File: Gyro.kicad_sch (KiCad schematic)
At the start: 5 parts, among them U4 MPU-6050

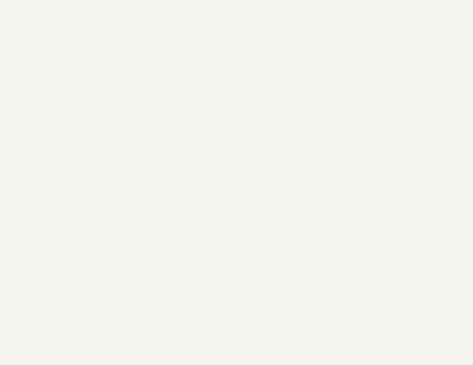
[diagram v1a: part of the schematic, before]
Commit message: MCU interfaces are done! Check the Changes and Complete ERC modifications
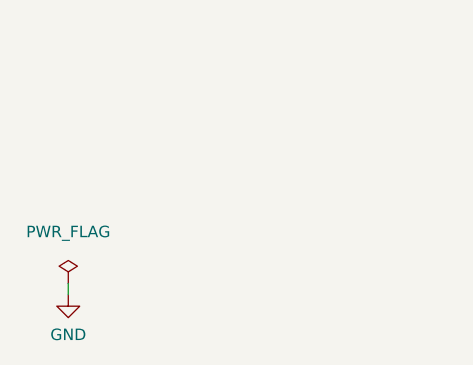
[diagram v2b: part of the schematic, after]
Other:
- company: (none) -> Parikshit Student Satellite Team
- title: (none) -> AOCS BOARD
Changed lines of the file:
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@@
 (kicad_sch (version 20211123) (generator eeschema)
   (paper "A4")
+  (title_block
+    (title "AOCS BOARD")
+    (company "Parikshit Student Satellite Team")
+  )
   (junction (at 113.03 90.17) (diameter 0) (color 0 0 0 0)
   )
@@
   (no_connect (at 151.13 74.93))
   (no_connect (at 151.13 80.01))
+  (wire (pts (xy 27.94 147.32) (xy 27.94 146.05))
+    (stroke (width 0) (type default) (color 0 0 0 0))
+  )
   (wire (pts (xy 114.3 43.18) (xy 114.3 46.99))
     (stroke (width 0) (type default) (color 0 0 0 0))
@@
       (effects (font (size 1.27 1.27)) hide)
     )
+    (pin "1")
+  )
+  (symbol (lib_id "power:PWR_FLAG") (at 27.94 146.05 0) (unit 1)
+    (in_bom yes) (on_board yes) (fields_autoplaced)
+    (property "Reference" "#FLG0107" (id 0) (at 27.94 144.145 0)
+      (effects (font (size 1.27 1.27)) hide)
+    )
+    (property "Value" "PWR_FLAG" (id 1) (at 27.94 140.335 0))
+    (property "Footprint" "" (id 2) (at 27.94 146.05 0)
+      (effects (font (size 1.27 1.27)) hide)
+    )
+    (property "Datasheet" "~" (id 3) (at 27.94 146.05 0)
+      (effects (font (size 1.27 1.27)) hide)
+    )
+    (pin "1")
+  )
+  (symbol (lib_id "power:GND") (at 27.94 147.32 0) (unit 1)
+    (in_bom yes) (on_board yes) (fields_autoplaced)
+    (property "Reference" "#PWR0271" (id 0) (at 27.94 153.67 0)
+      (effects (font (size 1.27 1.27)) hide)
+    )
+    (property "Value" "GND" (id 1) (at 27.94 151.765 0))
+    (property "Footprint" "" (id 2) (at 27.94 147.32 0)
+      (effects (font (size 1.27 1.27)) hide)
+    )
+    (property "Datasheet" "" (id 3) (at 27.94 147.32 0)
+      (effects (font (size 1.27 1.27)) hide)
+    )

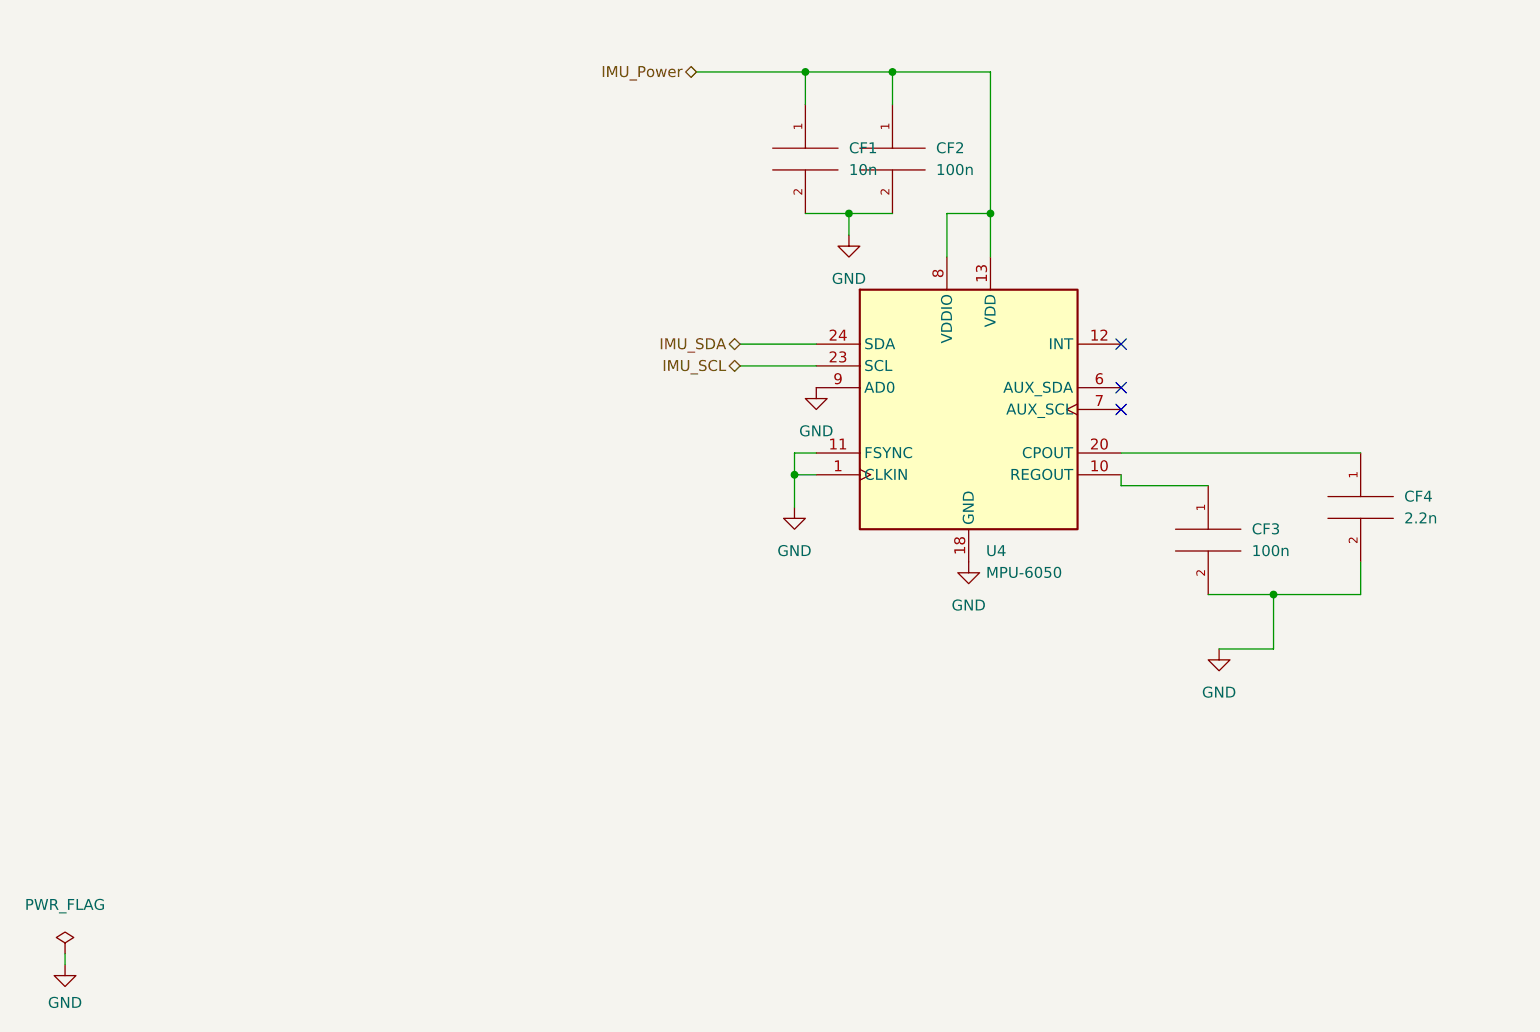
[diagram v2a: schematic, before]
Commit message: Max ERC errors corrected
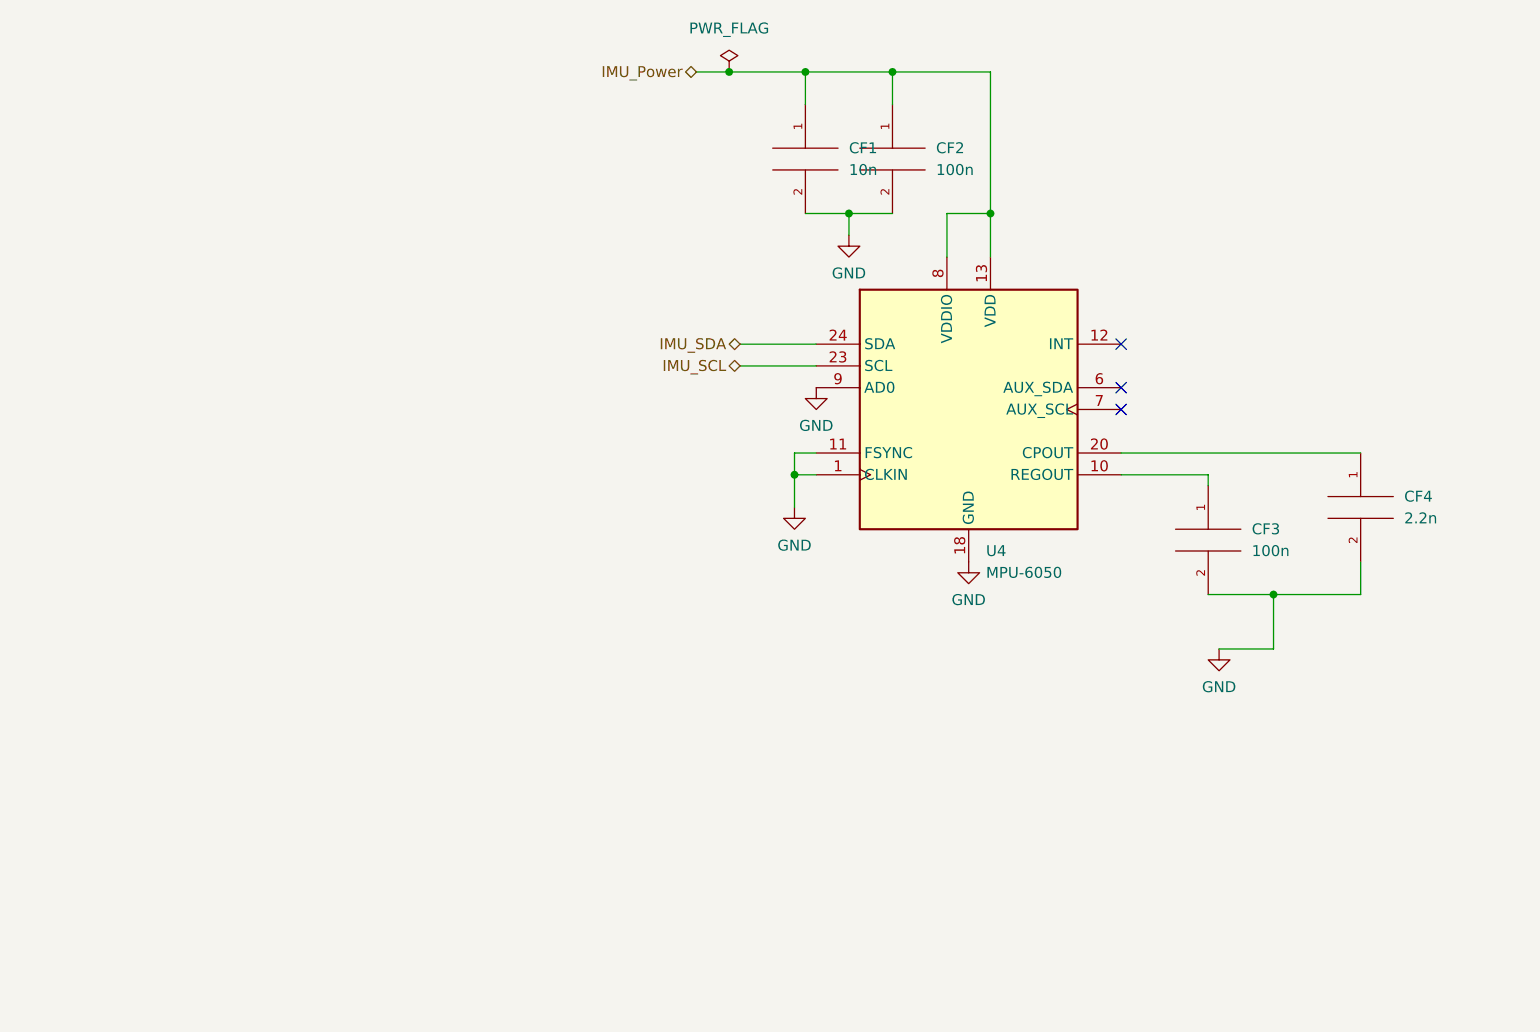
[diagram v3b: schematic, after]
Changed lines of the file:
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@@
   (junction (at 135.89 59.69) (diameter 0) (color 0 0 0 0)
+  )
+  (junction (at 105.41 43.18) (diameter 0) (color 0 0 0 0)
   )
   (junction (at 119.38 59.69) (diameter 0) (color 0 0 0 0)
@@
   (no_connect (at 151.13 74.93))
   (no_connect (at 151.13 80.01))
-  (wire (pts (xy 27.94 147.32) (xy 27.94 146.05))
-    (stroke (width 0) (type default) (color 0 0 0 0))
-  )
   (wire (pts (xy 114.3 43.18) (xy 114.3 46.99))
     (stroke (width 0) (type default) (color 0 0 0 0))
@@
     (stroke (width 0) (type default) (color 0 0 0 0))
   )
-  (wire (pts (xy 151.13 91.44) (xy 151.13 90.17))
-    (stroke (width 0) (type default) (color 0 0 0 0))
-  )
   (wire (pts (xy 114.3 59.69) (xy 119.38 59.69))
     (stroke (width 0) (type default) (color 0 0 0 0))
@@
     (stroke (width 0) (type default) (color 0 0 0 0))
   )
-  (wire (pts (xy 101.6 43.18) (xy 114.3 43.18))
+  (wire (pts (xy 101.6 43.18) (xy 105.41 43.18))
     (stroke (width 0) (type default) (color 0 0 0 0))
   )
@@
     (stroke (width 0) (type default) (color 0 0 0 0))
   )
+  (wire (pts (xy 105.41 43.18) (xy 114.3 43.18))
+    (stroke (width 0) (type default) (color 0 0 0 0))
+  )
   (wire (pts (xy 151.13 87.63) (xy 179.07 87.63))
     (stroke (width 0) (type default) (color 0 0 0 0))
@@
     (stroke (width 0) (type default) (color 0 0 0 0))
   )
-  (wire (pts (xy 161.29 91.44) (xy 151.13 91.44))
+  (wire (pts (xy 161.29 90.17) (xy 161.29 91.44))
+    (stroke (width 0) (type default) (color 0 0 0 0))
+  )
+  (wire (pts (xy 161.29 90.17) (xy 151.13 90.17))
     (stroke (width 0) (type default) (color 0 0 0 0))
   )
@@
     (pin "2")
   )
+  (symbol (lib_id "upsat-comms-hardware:GND") (at 162.56 110.49 0) (unit 1)
+    (in_bom yes) (on_board yes) (fields_autoplaced)
+    (property "Reference" "#PWR0163" (id 0) (at 162.56 116.84 0)
+      (effects (font (size 1.27 1.27)) hide)
+    )
+    (property "Value" "GND" (id 1) (at 162.56 114.935 0))
+    (property "Footprint" "" (id 2) (at 162.56 110.49 0))
+    (property "Datasheet" "" (id 3) (at 162.56 110.49 0))
+    (pin "1")
+  )
   (symbol (lib_id "pspice:C") (at 124.46 53.34 0) (unit 1)
     (in_bom yes) (on_board yes) (fields_autoplaced)
@@
     (pin "2")
   )
-  (symbol (lib_id "power:GND") (at 115.57 80.01 0) (unit 1)
-    (in_bom yes) (on_board yes) (fields_autoplaced)
-    (property "Reference" "#PWR0163" (id 0) (at 115.57 86.36 0)
-      (effects (font (size 1.27 1.27)) hide)
-    )
-    (property "Value" "GND" (id 1) (at 115.57 85.09 0))
-    (property "Footprint" "" (id 2) (at 115.57 80.01 0)
-      (effects (font (size 1.27 1.27)) hide)
-    )
-    (property "Datasheet" "" (id 3) (at 115.57 80.01 0)
-      (effects (font (size 1.27 1.27)) hide)
-    )
+  (symbol (lib_id "power:PWR_FLAG") (at 105.41 43.18 0) (unit 1)
+    (in_bom yes) (on_board yes) (fields_autoplaced)
+    (property "Reference" "#FLG0105" (id 0) (at 105.41 41.275 0)
+      (effects (font (size 1.27 1.27)) hide)
+    )
+    (property "Value" "PWR_FLAG" (id 1) (at 105.41 38.1 0))
+    (property "Footprint" "" (id 2) (at 105.41 43.18 0)
+      (effects (font (size 1.27 1.27)) hide)
+    )
+    (property "Datasheet" "~" (id 3) (at 105.41 43.18 0)
+      (effects (font (size 1.27 1.27)) hide)
+    )
+    (pin "1")
+  )
+  (symbol (lib_id "upsat-comms-hardware:GND") (at 113.03 93.98 0) (unit 1)
+    (in_bom yes) (on_board yes) (fields_autoplaced)
+    (property "Reference" "#PWR0166" (id 0) (at 113.03 100.33 0)
+      (effects (font (size 1.27 1.27)) hide)
+    )
+    (property "Value" "GND" (id 1) (at 113.03 98.425 0))
+    (property "Footprint" "" (id 2) (at 113.03 93.98 0))
+    (property "Datasheet" "" (id 3) (at 113.03 93.98 0))
+    (pin "1")
+  )
+  (symbol (lib_id "upsat-comms-hardware:GND") (at 115.57 80.01 0) (unit 1)
+    (in_bom yes) (on_board yes) (fields_autoplaced)
+    (property "Reference" "#PWR0165" (id 0) (at 115.57 86.36 0)
+      (effects (font (size 1.27 1.27)) hide)
+    )
+    (property "Value" "GND" (id 1) (at 115.57 84.455 0))
+    (property "Footprint" "" (id 2) (at 115.57 80.01 0))
+    (property "Datasheet" "" (id 3) (at 115.57 80.01 0))
     (pin "1")
   )
@@
     (pin "2")
   )
-  (symbol (lib_id "power:GND") (at 162.56 110.49 0) (unit 1)
-    (in_bom yes) (on_board yes) (fields_autoplaced)
-    (property "Reference" "#PWR0164" (id 0) (at 162.56 116.84 0)
-      (effects (font (size 1.27 1.27)) hide)
-    )
-    (property "Value" "GND" (id 1) (at 162.56 115.57 0))
-    (property "Footprint" "" (id 2) (at 162.56 110.49 0)
-      (effects (font (size 1.27 1.27)) hide)
-    )
-    (property "Datasheet" "" (id 3) (at 162.56 110.49 0)
-      (effects (font (size 1.27 1.27)) hide)
-    )
-    (pin "1")
-  )
-  (symbol (lib_id "power:GND") (at 133.35 100.33 0) (unit 1)
-    (in_bom yes) (on_board yes) (fields_autoplaced)
-    (property "Reference" "#PWR0166" (id 0) (at 133.35 106.68 0)
-      (effects (font (size 1.27 1.27)) hide)
-    )
-    (property "Value" "GND" (id 1) (at 133.35 105.41 0))
-    (property "Footprint" "" (id 2) (at 133.35 100.33 0)
-      (effects (font (size 1.27 1.27)) hide)
-    )
-    (property "Datasheet" "" (id 3) (at 133.35 100.33 0)
-      (effects (font (size 1.27 1.27)) hide)
-    )
-    (pin "1")
-  )
-  (symbol (lib_id "power:GND") (at 119.38 62.23 0) (unit 1)
+  (symbol (lib_id "upsat-comms-hardware:GND") (at 119.38 62.23 0) (unit 1)
     (in_bom yes) (on_board yes) (fields_autoplaced)
     (property "Reference" "#PWR0162" (id 0) (at 119.38 68.58 0)
       (effects (font (size 1.27 1.27)) hide)
     )
-    (property "Value" "GND" (id 1) (at 119.38 67.31 0))
-    (property "Footprint" "" (id 2) (at 119.38 62.23 0)
-      (effects (font (size 1.27 1.27)) hide)
-    )
-    (property "Datasheet" "" (id 3) (at 119.38 62.23 0)
-      (effects (font (size 1.27 1.27)) hide)
-    )
-    (pin "1")
-  )
-  (symbol (lib_id "power:GND") (at 113.03 93.98 0) (unit 1)
-    (in_bom yes) (on_board yes) (fields_autoplaced)
-    (property "Reference" "#PWR0165" (id 0) (at 113.03 100.33 0)
-      (effects (font (size 1.27 1.27)) hide)
-    )
-    (property "Value" "GND" (id 1) (at 113.03 99.06 0))
-    (property "Footprint" "" (id 2) (at 113.03 93.98 0)
-      (effects (font (size 1.27 1.27)) hide)
-    )
-    (property "Datasheet" "" (id 3) (at 113.03 93.98 0)
-      (effects (font (size 1.27 1.27)) hide)
-    )
-    (pin "1")
-  )
-  (symbol (lib_id "power:PWR_FLAG") (at 27.94 146.05 0) (unit 1)
-    (in_bom yes) (on_board yes) (fields_autoplaced)
-    (property "Reference" "#FLG0107" (id 0) (at 27.94 144.145 0)
-      (effects (font (size 1.27 1.27)) hide)
-    )
-    (property "Value" "PWR_FLAG" (id 1) (at 27.94 140.335 0))
-    (property "Footprint" "" (id 2) (at 27.94 146.05 0)
-      (effects (font (size 1.27 1.27)) hide)
-    )
-    (property "Datasheet" "~" (id 3) (at 27.94 146.05 0)
-      (effects (font (size 1.27 1.27)) hide)
-    )
-    (pin "1")
-  )
-  (symbol (lib_id "power:GND") (at 27.94 147.32 0) (unit 1)
-    (in_bom yes) (on_board yes) (fields_autoplaced)
-    (property "Reference" "#PWR0271" (id 0) (at 27.94 153.67 0)
-      (effects (font (size 1.27 1.27)) hide)
-    )
-    (property "Value" "GND" (id 1) (at 27.94 151.765 0))
-    (property "Footprint" "" (id 2) (at 27.94 147.32 0)
-      (effects (font (size 1.27 1.27)) hide)
-    )
-    (property "Datasheet" "" (id 3) (at 27.94 147.32 0)
-      (effects (font (size 1.27 1.27)) hide)
-    )
-    (pin "1")
-  )
+    (property "Value" "GND" (id 1) (at 119.38 66.675 0))
+    (property "Footprint" "" (id 2) (at 119.38 62.23 0))
+    (property "Datasheet" "" (id 3) (at 119.38 62.23 0))
+    (pin "1")
+  )
+  (symbol (lib_id "upsat-comms-hardware:GND") (at 133.35 100.33 0) (unit 1)
+    (in_bom yes) (on_board yes) (fields_autoplaced)
+    (property "Reference" "#PWR0164" (id 0) (at 133.35 106.68 0)
+      (effects (font (size 1.27 1.27)) hide)
+    )
+    (property "Value" "GND" (id 1) (at 133.35 104.775 0))
+    (property "Footprint" "" (id 2) (at 133.35 100.33 0))
+    (property "Datasheet" "" (id 3) (at 133.35 100.33 0))
+    (pin "1")
+  )

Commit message: Updated the changes
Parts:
- renumbered CF4 to CF3, CF3 to CF4
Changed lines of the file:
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@@
   (symbol (lib_id "pspice:C") (at 161.29 97.79 0) (unit 1)
     (in_bom yes) (on_board yes) (fields_autoplaced)
-    (property "Reference" "CF3" (id 0) (at 166.37 96.5199 0)
+    (property "Reference" "CF4" (id 0) (at 166.37 96.5199 0)
       (effects (font (size 1.27 1.27)) (justify left))
     )
@@
   (symbol (lib_id "upsat-comms-hardware:GND") (at 162.56 110.49 0) (unit 1)
     (in_bom yes) (on_board yes) (fields_autoplaced)
-    (property "Reference" "#PWR0163" (id 0) (at 162.56 116.84 0)
+    (property "Reference" "#PWR069" (id 0) (at 162.56 116.84 0)
       (effects (font (size 1.27 1.27)) hide)
     )
@@
   (symbol (lib_id "power:PWR_FLAG") (at 105.41 43.18 0) (unit 1)
     (in_bom yes) (on_board yes) (fields_autoplaced)
-    (property "Reference" "#FLG0105" (id 0) (at 105.41 41.275 0)
+    (property "Reference" "#FLG010" (id 0) (at 105.41 41.275 0)
       (effects (font (size 1.27 1.27)) hide)
     )
@@
   (symbol (lib_id "upsat-comms-hardware:GND") (at 113.03 93.98 0) (unit 1)
     (in_bom yes) (on_board yes) (fields_autoplaced)
-    (property "Reference" "#PWR0166" (id 0) (at 113.03 100.33 0)
+    (property "Reference" "#PWR067" (id 0) (at 113.03 100.33 0)
       (effects (font (size 1.27 1.27)) hide)
     )
@@
   (symbol (lib_id "upsat-comms-hardware:GND") (at 115.57 80.01 0) (unit 1)
     (in_bom yes) (on_board yes) (fields_autoplaced)
-    (property "Reference" "#PWR0165" (id 0) (at 115.57 86.36 0)
+    (property "Reference" "#PWR066" (id 0) (at 115.57 86.36 0)
       (effects (font (size 1.27 1.27)) hide)
     )
@@
   (symbol (lib_id "pspice:C") (at 179.07 93.98 0) (unit 1)
     (in_bom yes) (on_board yes) (fields_autoplaced)
-    (property "Reference" "CF4" (id 0) (at 184.15 92.7099 0)
+    (property "Reference" "CF3" (id 0) (at 184.15 92.7099 0)
       (effects (font (size 1.27 1.27)) (justify left))
     )
@@
   (symbol (lib_id "upsat-comms-hardware:GND") (at 119.38 62.23 0) (unit 1)
     (in_bom yes) (on_board yes) (fields_autoplaced)
-    (property "Reference" "#PWR0162" (id 0) (at 119.38 68.58 0)
+    (property "Reference" "#PWR065" (id 0) (at 119.38 68.58 0)
       (effects (font (size 1.27 1.27)) hide)
     )
@@
   (symbol (lib_id "upsat-comms-hardware:GND") (at 133.35 100.33 0) (unit 1)
     (in_bom yes) (on_board yes) (fields_autoplaced)
-    (property "Reference" "#PWR0164" (id 0) (at 133.35 106.68 0)
+    (property "Reference" "#PWR068" (id 0) (at 133.35 106.68 0)
       (effects (font (size 1.27 1.27)) hide)
     )
